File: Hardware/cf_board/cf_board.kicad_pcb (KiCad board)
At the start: 2 copper layers, 80.8 x 60.1 mm, 18 parts, among them J1 Conn_01x40, J2 Conn_02x26_Top_Bottom, J3 Conn_01x02, U1 74HC00

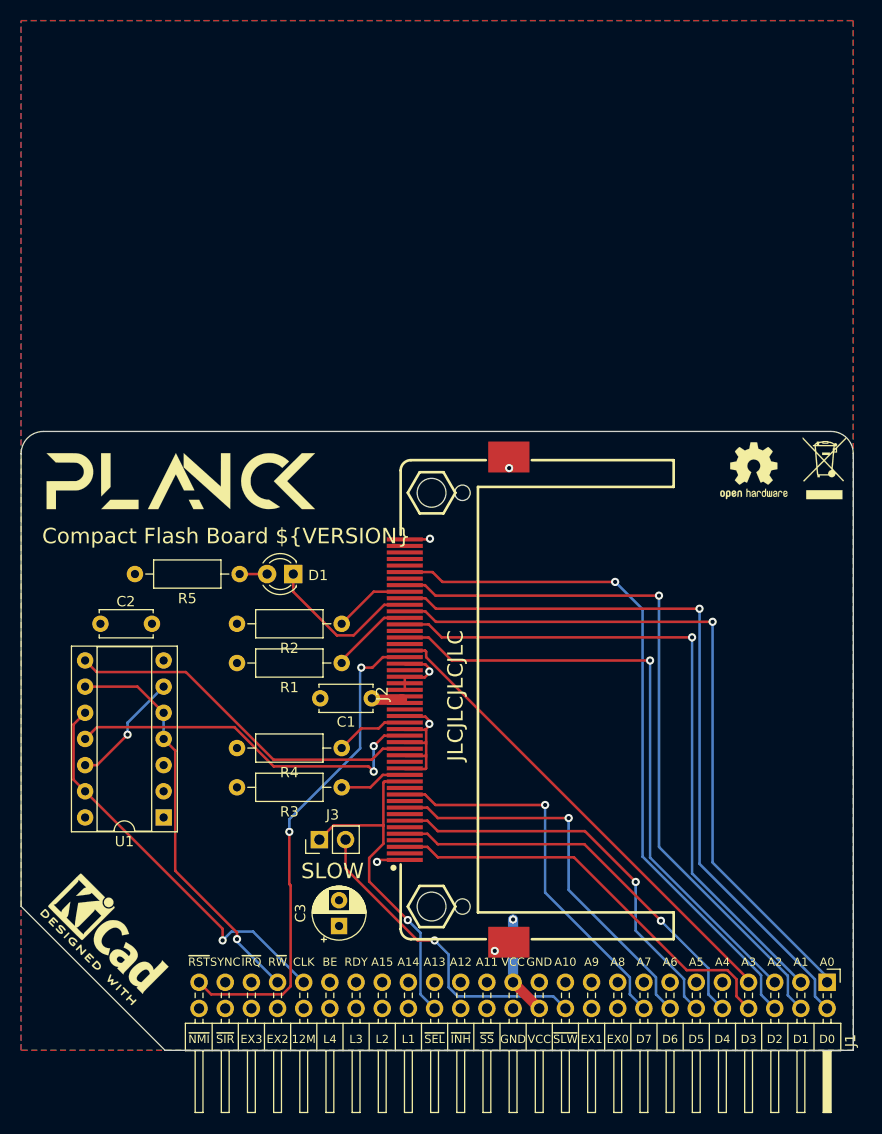
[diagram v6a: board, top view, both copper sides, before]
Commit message: move cf socket so that it is easier to extract
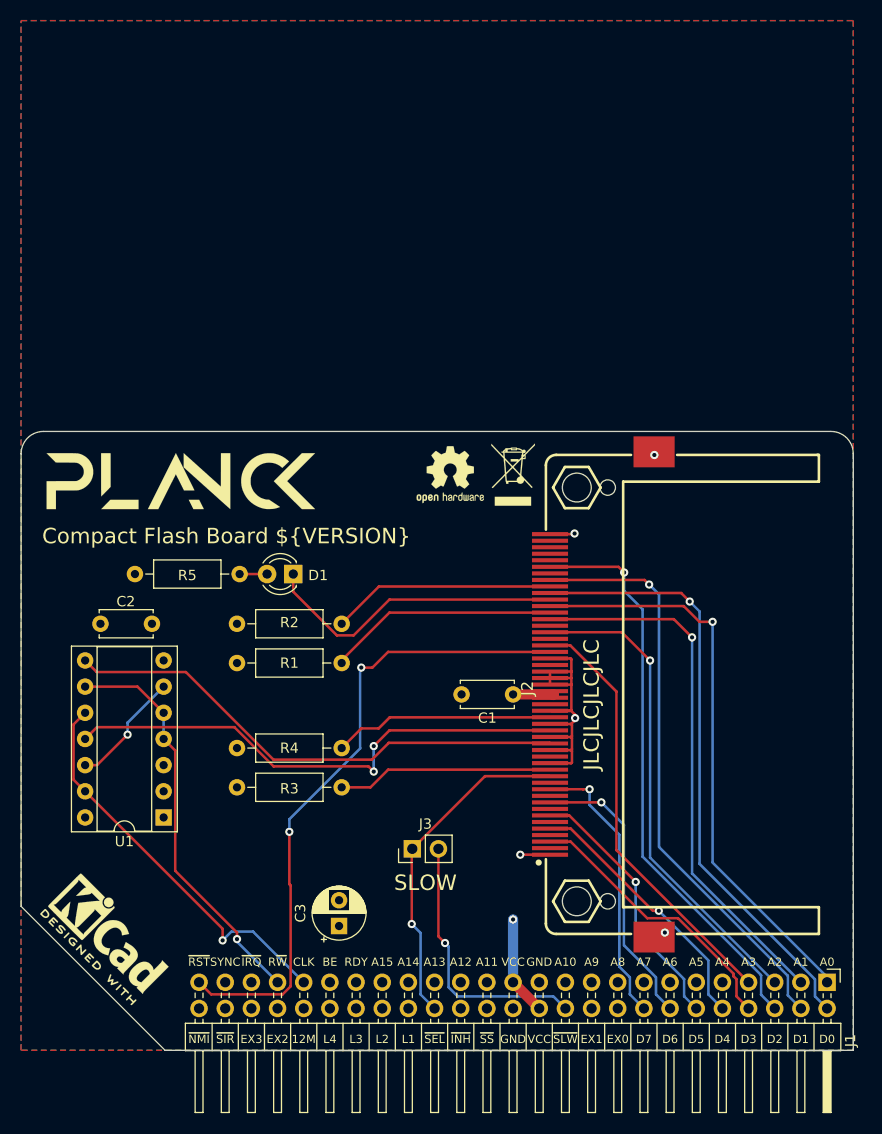
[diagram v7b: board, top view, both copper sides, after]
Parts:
- moved REF** 30.2 mm to (127.1, 62.7)
- moved REF** 29.5 mm to (121.0, 62.7)
- moved J2 14.1 mm to (135.8, 84.1)
- moved C1 13.7 mm to (127.1, 84.1)
- moved J3 9.06 mm to (117.3, 99.1)
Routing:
- net Net-(J2-Pad34): track 35.5 -> 49.8 mm
- net Net-(J2-Pad44): track 8.09 -> 22.4 mm
- net Net-(J2-Pad46): track 7.42 -> 21.7 mm
- net Net-(J2-Pad32): track 6.63 -> 20.9 mm
- net ~{RESET}: track 48.2 -> 62.5 mm
- net Net-(J2-Pad36): track 7.15 -> 21.5 mm
- net Net-(J2-Pad35): track 36.2 -> 50.5 mm
- net Net-(D1-Pad1): track 15.5 -> 29.8 mm
- net D0: track 73.0 -> 58.9 mm
- net A1: track 66.3 -> 52.4 mm
- net D5: track 39.6 -> 25.7 mm
- net A0: track 69.9 -> 56.0 mm
- net A2: track 61.0 -> 47.1 mm
- net D1: track 70.9 -> 57.1 mm
- net D3: track 40.8 -> 27.1 mm
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
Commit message: fix ERC
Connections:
- net Net-(D1-Pad1) renamed /~{SPKR}
- net Net-(J2-Pad32) renamed /~{CS1}
- net Net-(J2-Pad34) renamed /~{IO_RD}
- net Net-(J2-Pad35) renamed /~{IO_WR}
- net Net-(J2-Pad36) renamed /~{WE}
- net Net-(J2-Pad44) renamed /~{REG}
- net Net-(J2-Pad46) renamed /~{STSCHG}
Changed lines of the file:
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@@
   (net 47 "~{SSEL}")
   (net 48 "~{SLOW}")
-  (net 49 "Net-(D1-Pad1)")
+  (net 49 "/~{SPKR}")
   (net 50 "Net-(D1-Pad2)")
   (net 51 "unconnected-(J2-Pad24)")
@@
   (net 57 "unconnected-(J2-Pad30)")
   (net 58 "unconnected-(J2-Pad31)")
-  (net 59 "Net-(J2-Pad32)")
+  (net 59 "/~{CS1}")
   (net 60 "unconnected-(J2-Pad33)")
-  (net 61 "Net-(J2-Pad34)")
-  (net 62 "Net-(J2-Pad35)")
-  (net 63 "Net-(J2-Pad36)")
+  (net 61 "/~{IO_RD}")
+  (net 62 "/~{IO_WR}")
+  (net 63 "/~{WE}")
   (net 64 "unconnected-(J2-Pad37)")
   (net 65 "unconnected-(J2-Pad40)")
   (net 66 "unconnected-(J2-Pad42)")
   (net 67 "unconnected-(J2-Pad43)")
-  (net 68 "Net-(J2-Pad44)")
-  (net 69 "Net-(J2-Pad46)")
+  (net 68 "/~{REG}")
+  (net 69 "/~{STSCHG}")
   (net 70 "unconnected-(J2-Pad47)")
   (net 71 "unconnected-(J2-Pad48)")
@@
     (fp_line (start 0 0) (end 1.93 0) (layer "F.Fab") (width 0.1))
     (pad "1" thru_hole circle (at 0 0 180) (size 1.6 1.6) (drill 0.8) (layers *.Cu *.Mask)
-      (net 59 "Net-(J2-Pad32)") (pintype "passive"))
+      (net 59 "/~{CS1}") (pintype "passive"))
     (pad "2" thru_hole oval (at 10.16 0 180) (size 1.6 1.6) (drill 0.8) (layers *.Cu *.Mask)
       (net 8 "+5V") (pintype "passive"))
@@
       (net 58 "unconnected-(J2-Pad31)") (pinfunction "Pin_31") (pintype "passive"))
     (pad "32" smd rect (at -7.302 -5.05 180) (size 3.5 0.4) (layers "F.Cu" "F.Paste" "F.Mask")
-      (net 59 "Net-(J2-Pad32)") (pinfunction "Pin_32") (pintype "passive"))
+      (net 59 "/~{CS1}") (pinfunction "Pin_32") (pintype "passive"))
     (pad "33" smd rect (at -6.032 -5.05 180) (size 3.5 0.4) (layers "F.Cu" "F.Paste" "F.Mask")
       (net 60 "unconnected-(J2-Pad33)") (pinfunction "Pin_33") (pintype "passive"))
     (pad "34" smd rect (at -4.762 -5.05 180) (size 3.5 0.4) (layers "F.Cu" "F.Paste" "F.Mask")
-      (net 61 "Net-(J2-Pad34)") (pinfunction "Pin_34") (pintype "passive"))
+      (net 61 "/~{IO_RD}") (pinfunction "Pin_34") (pintype "passive"))
     (pad "35" smd rect (at -3.492 -5.05 180) (size 3.5 0.4) (layers "F.Cu" "F.Paste" "F.Mask")
-      (net 62 "Net-(J2-Pad35)") (pinfunction "Pin_35") (pintype "passive"))
+      (net 62 "/~{IO_WR}") (pinfunction "Pin_35") (pintype "passive"))
     (pad "36" smd rect (at -2.222 -5.05 180) (size 3.5 0.4) (layers "F.Cu" "F.Paste" "F.Mask")
-      (net 63 "Net-(J2-Pad36)") (pinfunction "Pin_36") (pintype "passive"))
+      (net 63 "/~{WE}") (pinfunction "Pin_36") (pintype "passive"))
     (pad "37" smd rect (at -0.952 -5.05 180) (size 3.5 0.4) (layers "F.Cu" "F.Paste" "F.Mask")
       (net 64 "unconnected-(J2-Pad37)") (pinfunction "Pin_37") (pintype "passive"))
@@
       (net 67 "unconnected-(J2-Pad43)") (pinfunction "Pin_43") (pintype "passive"))
     (pad "44" smd rect (at 7.938 -5.05 180) (size 3.5 0.4) (layers "F.Cu" "F.Paste" "F.Mask")
-      (net 68 "Net-(J2-Pad44)") (pinfunction "Pin_44") (pintype "passive"))
+      (net 68 "/~{REG}") (pinfunction "Pin_44") (pintype "passive"))
     (pad "45" smd rect (at 9.208 -5.05 180) (size 3.5 0.4) (layers "F.Cu" "F.Paste" "F.Mask")
-      (net 49 "Net-(D1-Pad1)") (pinfunction "Pin_45") (pintype "passive"))
+      (net 49 "/~{SPKR}") (pinfunction "Pin_45") (pintype "passive"))
     (pad "46" smd rect (at 10.478 -5.05 180) (size 3.5 0.4) (layers "F.Cu" "F.Paste" "F.Mask")
-      (net 69 "Net-(J2-Pad46)") (pinfunction "Pin_46") (pintype "passive"))
+      (net 69 "/~{STSCHG}") (pinfunction "Pin_46") (pintype "passive"))
     (pad "47" smd rect (at 11.748 -5.05 180) (size 3.5 0.4) (layers "F.Cu" "F.Paste" "F.Mask")
       (net 70 "unconnected-(J2-Pad47)") (pinfunction "Pin_47") (pintype "passive"))
@@
     (fp_line (start 0 0) (end 1.93 0) (layer "F.Fab") (width 0.1))
     (pad "1" thru_hole circle (at 0 0 180) (size 1.6 1.6) (drill 0.8) (layers *.Cu *.Mask)
-      (net 69 "Net-(J2-Pad46)") (pintype "passive"))
+      (net 69 "/~{STSCHG}") (pintype "passive"))
     (pad "2" thru_hole oval (at 10.16 0 180) (size 1.6 1.6) (drill 0.8) (layers *.Cu *.Mask)
       (net 8 "+5V") (pintype "passive"))
@@
     (fp_line (start 8.23 -1.25) (end 1.93 -1.25) (layer "F.Fab") (width 0.1))
     (pad "1" thru_hole circle (at 0 0 180) (size 1.6 1.6) (drill 0.8) (layers *.Cu *.Mask)
-      (net 68 "Net-(J2-Pad44)") (pintype "passive"))
+      (net 68 "/~{REG}") (pintype "passive"))
     (pad "2" thru_hole oval (at 10.16 0 180) (size 1.6 1.6) (drill 0.8) (layers *.Cu *.Mask)
       (net 8 "+5V") (pintype "passive"))
@@
       (net 7 "GND") (pinfunction "GND") (pintype "power_in"))
     (pad "8" thru_hole oval (at 7.62 15.24 180) (size 1.6 1.6) (drill 0.8) (layers *.Cu *.Mask)
-      (net 61 "Net-(J2-Pad34)") (pintype "output"))
+      (net 61 "/~{IO_RD}") (pintype "output"))
     (pad "9" thru_hole oval (at 7.62 12.7 180) (size 1.6 1.6) (drill 0.8) (layers *.Cu *.Mask)
       (net 39 "R~{W}") (pintype "input"))
@@
       (net 28 "CLK") (pintype "input"))
     (pad "11" thru_hole oval (at 7.62 7.62 180) (size 1.6 1.6) (drill 0.8) (layers *.Cu *.Mask)
-      (net 62 "Net-(J2-Pad35)") (pintype "output"))
+      (net 62 "/~{IO_WR}") (pintype "output"))
     (pad "12" thru_hole oval (at 7.62 5.08 180) (size 1.6 1.6) (drill 0.8) (layers *.Cu *.Mask)
       (net 73 "Net-(U1-Pad12)") (pintype "input"))
@@
     (fp_circle (center 1.27 0) (end 2.77 0) (layer "F.Fab") (width 0.1) (fill none))
     (pad "1" thru_hole rect (at 0 0 180) (size 1.8 1.8) (drill 0.9) (layers *.Cu *.Mask)
-      (net 49 "Net-(D1-Pad1)") (pinfunction "K") (pintype "passive"))
+      (net 49 "/~{SPKR}") (pinfunction "K") (pintype "passive"))
     (pad "2" thru_hole circle (at 2.54 0 180) (size 1.8 1.8) (drill 0.9) (layers *.Cu *.Mask)
       (net 50 "Net-(D1-Pad2)") (pinfunction "A") (pintype "passive"))
@@
     (fp_line (start 8.23 -1.25) (end 1.93 -1.25) (layer "F.Fab") (width 0.1))
     (pad "1" thru_hole circle (at 0 0 180) (size 1.6 1.6) (drill 0.8) (layers *.Cu *.Mask)
-      (net 63 "Net-(J2-Pad36)") (pintype "passive"))
+      (net 63 "/~{WE}") (pintype "passive"))
     (pad "2" thru_hole oval (at 10.16 0 180) (size 1.6 1.6) (drill 0.8) (layers *.Cu *.Mask)
       (net 8 "+5V") (pintype "passive"))
